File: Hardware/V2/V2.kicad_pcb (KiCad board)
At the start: 2 copper layers, 68 parts, among them J1 USB_B_Mini, J2 I2C_OLED, J3 ICSP, Q1 MMBT2222, SW1 SW_Push, SW2 SW_Push, SW3 SW_Push, U1 ATmega32U4-AU, U2 LIS3DH, U3 DHT11, U4 AP2112K-3.3, Y1 16MHz

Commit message: Comenzando la placa
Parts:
- added D15: 1N4148, Diode_SMD:D_SOD-123, B.Cu at (144.8, 71.1)
- added J4: BT_CONN, Connector_PinHeader_2.54mm:PinHeader_1x06_P2.54mm_Vertical, F.Cu at (188.0, 63.5)
- added J5: BAT, Connector_JST:JST_PH_S2B-PH-SM4-TB_1x02-1MP_P2.00mm_Horizontal, B.Cu at (143.5, 63.5)
- C14, C15, C16, C17, C18, C19, D3, J1, U1, U4, Y1: moved to B.Cu
- moved BZ1 117.2 mm to (113.0, 66.0)
- moved D2 115.7 mm to (139.7, 63.5)
- moved C18 108.0 mm to (148.9, 78.7)
- moved R10 103.6 mm to (110.5, 109.2)
- moved D5 100.9 mm to (154.9, 63.5)
- moved D1 98.3 mm to (132.1, 63.5)
- moved D10 96.6 mm to (146.1, 101.6), turned to 90 degrees
- moved D9 95.5 mm to (153.7, 101.6), turned to 90 degrees
- moved C19 95.4 mm to (148.9, 88.9)
- moved U1 88.3 mm to (157.5, 85.1), turned to 90 degrees
- moved U4 82.5 mm to (160.0, 69.8), turned to 90 degrees
- moved C1 77.3 mm to (174.0, 83.5), turned to 90 degrees
- moved U2 76.0 mm to (177.7, 83.8), turned to 90 degrees
- moved D6 72.5 mm to (162.6, 63.5)
- moved D8 71.4 mm to (160.0, 101.6), turned to 90 degrees
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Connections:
- J2 pad 4: SCL -> SDA
- R4 pad 1: SCL -> SDA
- U1 pad 19: SCL -> SDA
- U2 pad 6: SCL -> SDA
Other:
- board outline added: 101.6 x 57.1 mm

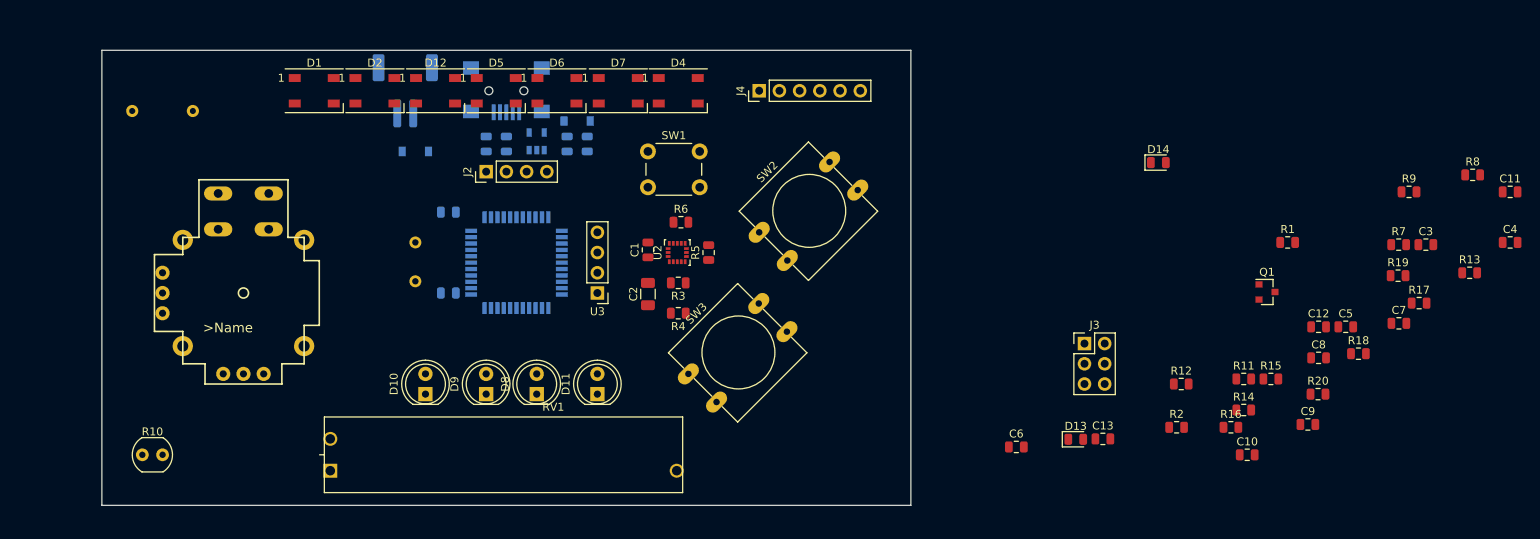
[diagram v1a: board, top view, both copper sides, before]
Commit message: Componentes colocados
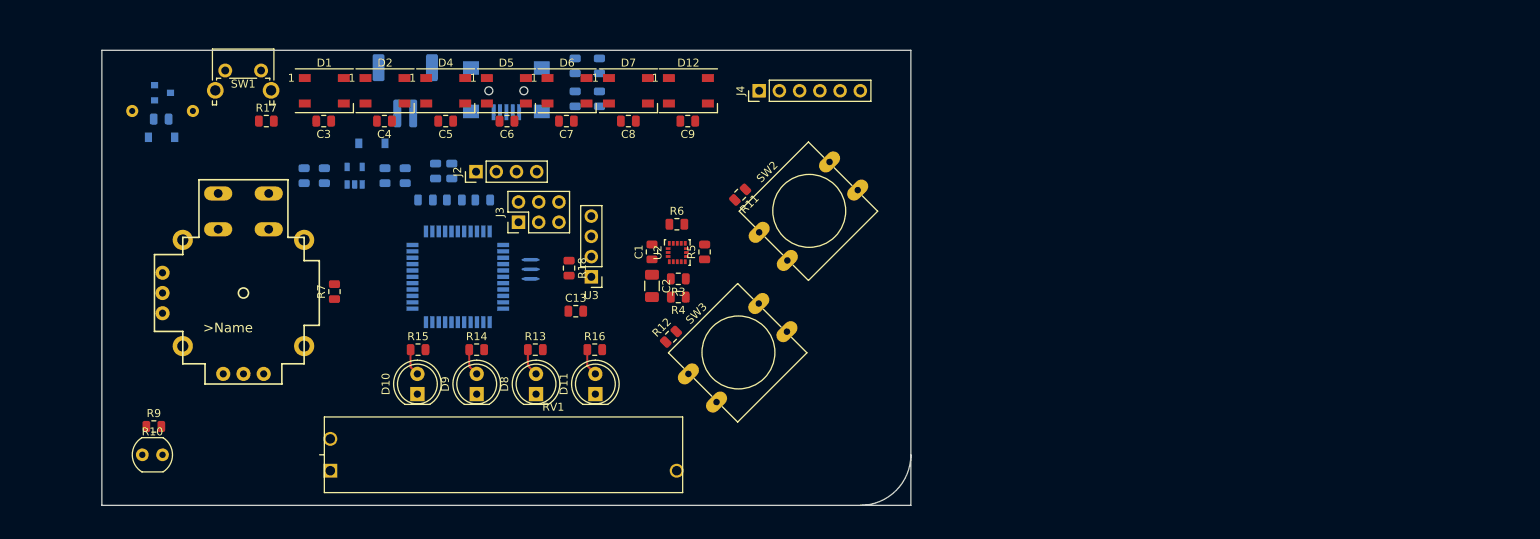
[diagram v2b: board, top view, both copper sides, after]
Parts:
- removed C18, C19: 22pF, Capacitor_SMD:C_0805_2012Metric
- C10, C11, C12, D13, D14, Q1, R1, R19, R2, R20, R8: moved to B.Cu
- SW1: footprint Button_Switch_THT:SW_PUSH_6mm -> Button_Switch_THT:SW_Tactile_SPST_Angled_PTS645Vx39-2LFS
- Y1: footprint Crystal:Crystal_HC49-4H_Vertical -> lib_fp:RESONATOR-SMD-3.2X1.3
- moved R8 164.9 mm to (112.9, 67.1)
- moved R9 160.4 mm to (111.9, 105.7)
- moved R17 146.6 mm to (126.1, 67.3)
- moved C4 142.2 mm to (140.9, 67.3), turned to 180 degrees
- moved Q1 140.9 mm to (113.0, 63.8)
- moved C3 139.3 mm to (133.3, 67.3), turned to 180 degrees
- moved C11 136.2 mm to (146.1, 77.2)
- moved R7 133.8 mm to (134.6, 88.7), turned to 90 degrees
- moved R13 117.7 mm to (159.8, 96.0)
- moved C5 115.9 mm to (148.6, 67.3), turned to 180 degrees
- moved C7 107.6 mm to (163.8, 67.3), turned to 180 degrees
- moved R15 107.2 mm to (145.1, 96.0)
- moved C12 106.2 mm to (153.2, 77.2), turned to 180 degrees
- moved R19 105.7 mm to (164.8, 64.5), turned to 90 degrees
- moved R1 105.4 mm to (149.4, 73.6), turned to 90 degrees
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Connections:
- U1 pad 16: Net-(C19-Pad1) -> Net-(U1-Pad16)
- Y1 pad 2: Net-(C19-Pad1) -> GND
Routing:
- net Net-(D8-Pad2): track 0.00 -> 3.47 mm
- net Net-(D11-Pad2): track 0.00 -> 3.47 mm
- net Net-(D9-Pad2): track 0.00 -> 3.44 mm
- net Net-(D10-Pad2): track 0.00 -> 3.40 mm
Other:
- outline, holes or cut-outs redrawn

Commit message: Enrutado comenzado
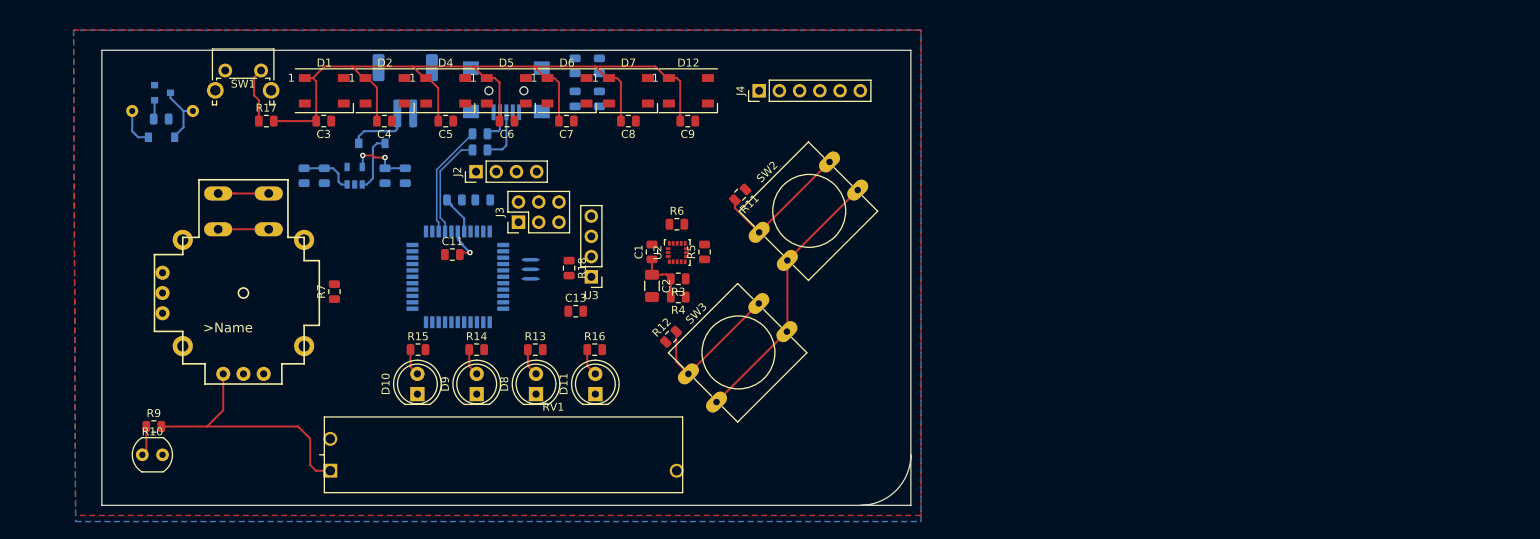
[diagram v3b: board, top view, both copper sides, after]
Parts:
- C11: moved to F.Cu
- moved C11 7.65 mm to (149.4, 84.1)
- moved R2 7.28 mm to (152.9, 68.9), turned to 0 degrees
- moved R1 4.42 mm to (152.9, 70.9), turned to 0 degrees
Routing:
- net +3V3: track 0.00 -> 201.2 mm, vias 0 -> 2
- net BTN1: track 0.00 -> 18.5 mm
- net BTN2: track 0.00 -> 17.8 mm
- net D-: track 0.00 -> 14.2 mm
- net VUSB: track 0.00 -> 14.1 mm
- net D+: track 0.00 -> 13.0 mm
- net Net-(D15-Pad2): track 0.00 -> 8.04 mm
- net Net-(BZ1-Pad2): track 0.00 -> 7.90 mm
- net RST: track 0.00 -> 6.96 mm
- net Net-(J1-Pad3): track 0.00 -> 6.77 mm
- net JOY-BTN: track 0.00 -> 6.35 mm
- net Net-(C10-Pad1): track 0.00 -> 4.85 mm
- net Net-(C11-Pad2): track 0.00 -> 4.66 mm, vias 0 -> 1
- net Net-(J1-Pad2): track 0.00 -> 3.96 mm
- net LDR: track 0.00 -> 3.77 mm
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- added copper zone on B.Cu, net GND
- added copper zone on F.Cu, net GND

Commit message: Cambio de forma
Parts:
- C13: moved to B.Cu
- moved BZ1 95.0 mm to (202.2, 98.8)
- moved D3 95.0 mm to (202.1, 102.1)
- moved Q1 95.0 mm to (202.2, 96.5)
- moved R8 95.0 mm to (202.0, 99.8)
- moved C13 25.6 mm to (140.3, 84.3), turned to 180 degrees
- moved J4 19.3 mm to (170.2, 71.1)
- moved C12 1.11 mm to (154.4, 77.2)
- moved C10 0.86 mm to (150.5, 77.2)
- moved Y1 0.51 mm to (159.5, 86.4)
- moved R19 0.08 mm to (164.8, 64.4), turned to 270 degrees
- moved R20 0.08 mm to (167.9, 64.4)
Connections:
- J4 pad 5: +5V -> +3V3
- U1 pad 20: /RXI -> BT_TX
- U1 pad 21: /TXO -> BT_RX
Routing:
- net +3V3: track 201.2 -> 378.2 mm, vias 2 -> 6
- net SDA: track 0.00 -> 71.3 mm, vias 0 -> 3
- net DHT: track 0.00 -> 68.3 mm, vias 0 -> 3
- net RST: track 6.96 -> 67.7 mm, vias 0 -> 2
- net SCL: track 0.00 -> 59.3 mm, vias 0 -> 3
- net LDR: track 3.77 -> 61.2 mm, vias 0 -> 1
- net BUZZ: track 0.00 -> 56.1 mm, vias 0 -> 2
- net BTN2: track 17.8 -> 70.1 mm, vias 0 -> 2
- net Net-(R20-Pad2): track 0.00 -> 38.6 mm
- net BT_TX: track 0.00 -> 36.5 mm, vias 0 -> 2
- net GND: track 0.00 -> 36.4 mm, vias 0 -> 10
- net BT_RX: track 0.00 -> 34.4 mm, vias 0 -> 2
- net JOY-V: track 0.00 -> 32.2 mm
- net NEO: track 0.00 -> 30.7 mm, vias 0 -> 1
- net JOY-H: track 0.00 -> 30.2 mm
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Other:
- board size 101.6 x 57.1 mm -> 115 x 61 mm
- rule trace_min: 0.1524 -> 0.127

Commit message: Placa enrutada
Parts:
- added REF**: MountingHole_3.2mm_M3, MountingHole:MountingHole_3.2mm_M3, F.Cu at (125.7, 61.5)
- added REF**: MountingHole_3.2mm_M3, MountingHole:MountingHole_3.2mm_M3, F.Cu at (187.5, 61.5)
- added REF**: MountingHole_3.2mm_M3, MountingHole:MountingHole_3.2mm_M3, F.Cu at (207.5, 110.0)
- added REF**: MountingHole_3.2mm_M3, MountingHole:MountingHole_3.2mm_M3, F.Cu at (105.2, 110.0)
- SW1: moved to B.Cu
- moved R17 5.85 mm to (121.8, 71.3), turned to 45 degrees
- moved SW1 5.68 mm to (119.9, 66.5), turned to 225 degrees
- moved J1 3.30 mm to (156.2, 60.2)
- moved J5 3.30 mm to (143.5, 60.2)
- moved D15 2.54 mm to (139.3, 67.6)
- moved R1 2.54 mm to (152.9, 68.4)
- moved R2 2.54 mm to (152.9, 66.4)
- moved D13 2.54 mm to (164.8, 57.8)
- moved D14 2.54 mm to (167.9, 57.8)
- moved R19 2.54 mm to (164.8, 61.9)
- moved R20 2.54 mm to (167.9, 61.9)
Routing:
- net +3V3: track 378.2 -> 400.7 mm, vias 6 -> 7
- net GND: track 36.4 -> 58.0 mm, vias 10 -> 16
- net BUZZ: track 56.1 -> 70.4 mm, vias 2 -> 0
- net Net-(R19-Pad2): track 25.8 -> 35.3 mm, vias 0 -> 4
- net Net-(D2-Pad2): track 21.0 -> 28.5 mm
- net Net-(D5-Pad2): track 18.8 -> 26.2 mm
- net VUSB: track 33.9 -> 38.9 mm
- net Net-(R20-Pad2): track 38.6 -> 42.3 mm
- net Net-(D6-Pad2): track 15.6 -> 19.2 mm
- net D-: track 14.2 -> 17.2 mm
- net D+: track 13.0 -> 15.6 mm
- net RST: track 67.7 -> 65.3 mm
- net Net-(D4-Pad2): track 21.7 -> 20.7 mm
- net Net-(D15-Pad2): track 8.04 -> 7.46 mm
- net Net-(J1-Pad2): track 3.96 -> 3.43 mm
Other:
- outline, holes or cut-outs redrawn

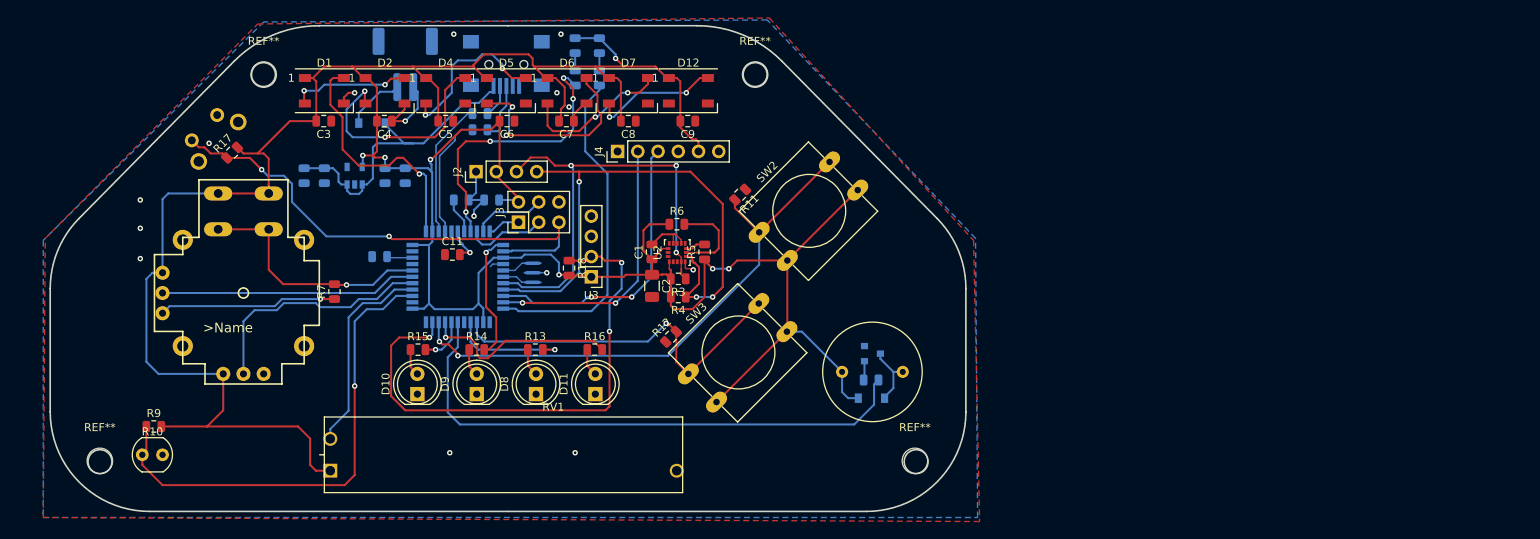
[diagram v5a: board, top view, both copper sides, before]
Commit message: Colocando lo componentes en 3D
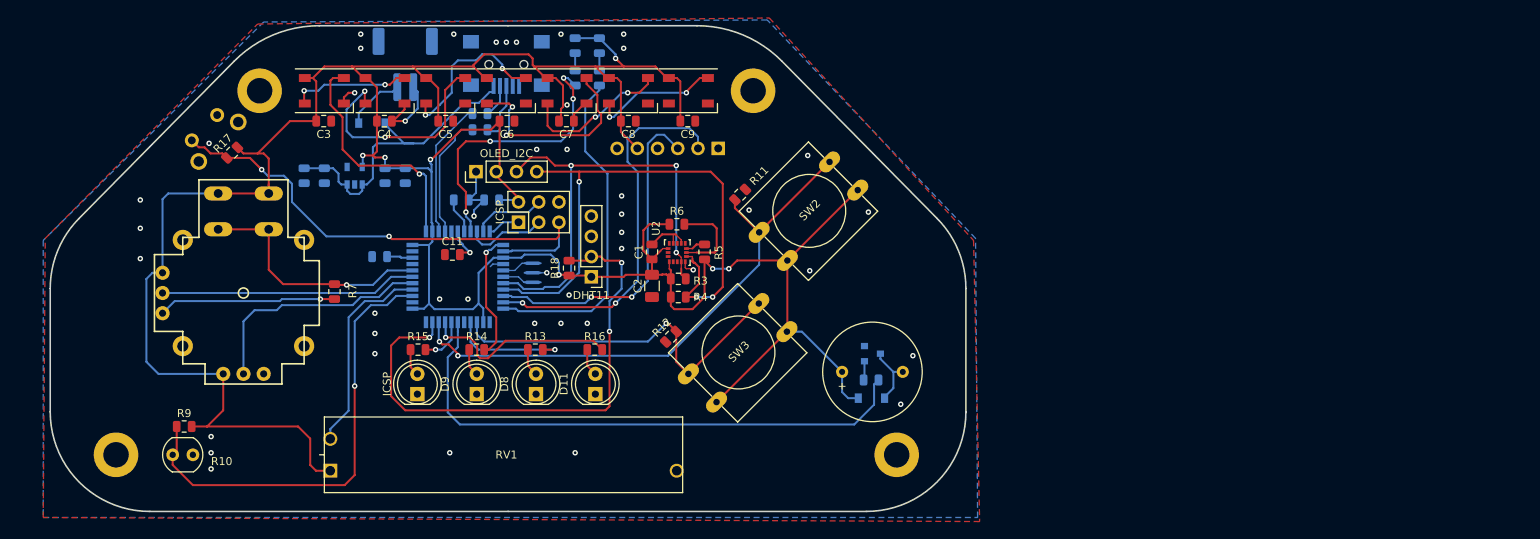
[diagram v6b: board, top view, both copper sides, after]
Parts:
- removed the REF** at (125.7, 61.5)
- removed the REF** at (187.5, 61.5)
- removed the REF** at (207.5, 110.0)
- removed the REF** at (105.2, 110.0)
- added REF**: MountingHole_3.2mm_M3_DIN965_Pad, MountingHole:MountingHole_3.2mm_M3_DIN965_Pad, F.Cu at (125.2, 63.5)
- added REF**: MountingHole_3.2mm_M3_DIN965_Pad, MountingHole:MountingHole_3.2mm_M3_DIN965_Pad, F.Cu at (107.2, 109.2)
- added REF**: MountingHole_3.2mm_M3_DIN965_Pad, MountingHole:MountingHole_3.2mm_M3_DIN965_Pad, F.Cu at (205.2, 109.2)
- added REF**: MountingHole_3.2mm_M3_DIN965_Pad, MountingHole:MountingHole_3.2mm_M3_DIN965_Pad, F.Cu at (187.2, 63.5)
- BT-HC05: renamed from J4; moved to B.Cu
- Battery - 3.7V: renamed from J5
- moved BT-HC05 12.6 mm to (182.8, 70.7)
- moved R10 3.81 mm to (114.3, 109.2)
- moved R9 3.81 mm to (115.7, 105.7)
- renumbered U3 to DHT11, D10 to ICSP, J3 to ICSP, J2 to OLED_I2C, SW1 to RESET
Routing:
- net BT_RX: track 34.4 -> 49.4 mm
- net BT_TX: track 36.5 -> 41.9 mm
- net +3V3: track 400.7 -> 395.9 mm
- net LDR: track 61.2 -> 57.4 mm
- net SDA: track 71.1 -> 72.8 mm
- net NEO: track 30.7 -> 29.9 mm
- net GND: vias 16 -> 46
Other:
- outline, holes or cut-outs redrawn
- board text added: "+"

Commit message: Trabajando en la serigrafía
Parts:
- removed the ICSP at (145.0, 101.6)
- added ?: , OLIMEX_LOGOs-FP:LOGO_OPENHARDWARE_8x8, F.Cu at (206.9, 84.7)
- added D9: LED_Y, LED_THT:LED_D5.0mm, F.Cu at (145.0, 101.6)
- added G***: LOGO, logos:logaso, B.Cu at (156.0, 112.2)
- added G***: LOGO, logos:bombilla, F.Cu at (111.5, 105.1)
- added REF**: KiCAD Logo, Symbol:Symbol_KiCAD-Logo_CopperAndSilkScreenTop, F.Cu at (191.3, 112.2)
- moved D10 14.9 mm to (152.5, 101.6)
- moved R16 14.9 mm to (152.4, 96.1), turned to 180 degrees
- moved D11 7.47 mm to (160.0, 101.6)
- moved D12 7.39 mm to (167.3, 101.6)
- moved R14 7.26 mm to (159.7, 96.0), turned to 180 degrees
- moved R13 7.21 mm to (167.1, 95.9), turned to 180 degrees
- moved RV1 0.83 mm to (133.3, 110.0)
- renumbered D11 to D10, D9 to D11, D8 to D12, D13 to RX, D14 to TX
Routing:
- net LED_G: track 24.8 -> 5.54 mm
- net LED_R: track 15.0 -> 17.3 mm, vias 1 -> 3
- net LED_B: track 16.2 -> 18.1 mm
- net GND: vias 46 -> 44
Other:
- board text added: "A0"
- board text added: "A1"
- board text added: "D13"
- board text added: "D4"
- board text added: "D5"
- board text added: "D7"
- board text added: "D8"
- board text added: "H-A2"
- board text added: "K-A4"
- board text added: "V-A3"
- board text added: "X"
- board text added: "Y"

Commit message: Guardado de seguridad
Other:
- board text added: "x"
- board text added: "y"
- board text added: "z"
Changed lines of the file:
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@@
   (general
     (thickness 1.6)
-    (drawings 52)
+    (drawings 66)
     (tracks 726)
     (zones 0)
@@
       (xy 0.175724 -1.548757)) (layer F.SilkS) (width 0.01))
   )
+  (gr_text z (at 174.879 75.184) (layer F.SilkS)
+    (effects (font (size 0.6 0.6) (thickness 0.127)))
+  )
+  (gr_text y (at 175.006 77.089) (layer F.SilkS)
+    (effects (font (size 0.6 0.6) (thickness 0.127)))
+  )
+  (gr_text x (at 176.784 75.438) (layer F.SilkS)
+    (effects (font (size 0.6 0.6) (thickness 0.127)))
+  )
+  (gr_line (start 177.292 76.2) (end 178.308 76.2) (layer F.SilkS) (width 0.127))
+  (gr_line (start 175.768 77.724) (end 175.768 78.74) (layer F.SilkS) (width 0.127))
+  (gr_line (start 175.26 75.692) (end 175.768 75.692) (layer F.SilkS) (width 0.127))
+  (gr_line (start 175.768 76.2) (end 175.26 75.692) (layer F.SilkS) (width 0.127))
+  (gr_line (start 175.26 75.692) (end 175.26 76.2) (layer F.SilkS) (width 0.127))
+  (gr_line (start 178.308 76.2) (end 177.292 75.692) (layer F.SilkS) (width 0.127))
+  (gr_line (start 177.292 76.708) (end 178.308 76.2) (layer F.SilkS) (width 0.127))
+  (gr_line (start 175.768 76.2) (end 177.292 76.2) (layer F.SilkS) (width 0.127))
+  (gr_line (start 175.768 77.724) (end 175.768 76.2) (layer F.SilkS) (width 0.127))
+  (gr_line (start 175.768 78.74) (end 176.276 77.724) (layer F.SilkS) (width 0.127))
+  (gr_line (start 175.26 77.724) (end 175.768 78.74) (layer F.SilkS) (width 0.127))
   (gr_text X (at 105.537 98.933) (layer F.SilkS)
     (effects (font (size 1 1) (thickness 0.2)))
@@
   (segment (start 125.125 73.055) (end 125.476 73.406) (width 0.254) (layer F.Cu) (net 29))
   (via (at 141.478 81.788) (size 0.6858) (drill 0.3302) (layers F.Cu B.Cu) (net 29))
-  (segment (start 141.820899 82.130899) (end 162.471101 82.130899) (width 0.254) (layer F.Cu) (net 29))
-  (segment (start 141.478 81.788) (end 141.820899 82.130899) (width 0.254) (layer F.Cu) (net 29))
-  (segment (start 162.814 81.788) (end 162.814 80.01) (width 0.254) (layer F.Cu) (net 29) (status 20))
-  (segment (start 162.471101 82.130899) (end 162.814 81.788) (width 0.254) (layer F.Cu) (net 29))
   (segment (start 133.604 81.788) (end 141.478 81.788) (width 0.254) (layer B.Cu) (net 29))
   (segment (start 126.238 74.168) (end 128.27 74.168) (width 0.254) (layer B.Cu) (net 29))
@@
   (segment (start 124.007826 71.937826) (end 125.476 73.406) (width 0.254) (layer F.Cu) (net 29))
   (segment (start 121.102174 71.937826) (end 124.007826 71.937826) (width 0.254) (layer F.Cu) (net 29) (status 10))
+  (segment (start 141.820899 82.130899) (end 162.471101 82.130899) (width 0.254) (layer F.Cu) (net 29))
+  (segment (start 141.478 81.788) (end 141.820899 82.130899) (width 0.254) (layer F.Cu) (net 29))
+  (segment (start 162.471101 82.130899) (end 162.814 81.788) (width 0.254) (layer F.Cu) (net 29))
+  (segment (start 162.814 81.788) (end 162.814 80.01) (width 0.254) (layer F.Cu) (net 29) (status 20))
   (segment (start 201.184 99.709) (end 201.071 99.822) (width 0.254) (layer B.Cu) (net 30) (status 30))
   (segment (start 201.184 97.47) (end 201.184 99.709) (width 0.254) (layer B.Cu) (net 30) (status 30))
